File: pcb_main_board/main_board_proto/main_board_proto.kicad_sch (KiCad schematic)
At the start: 35 parts, among them J1 Sortie Moteur 1, J10 L298N 2, J11 L298N 3, J12 IN M2, J13 IN M3, J14 Conn M2, J15 Conn M3, J16 Ardu_M2, J17 Ardu_M3, J18 Entree puissance, J19 output ext 2, J2 L298N 1, J20 button ON/OFF, J3 Conn M1, J4 Ardu_alim, J5 Output ext 1, J6 Ardu_M1, J7 IN M1, J8 Sortie Moteur 2, J9 Sortie Moteur 3, U1 TSR1-2450E, U2 TSR1-2450E, U3 TSR1-2450E

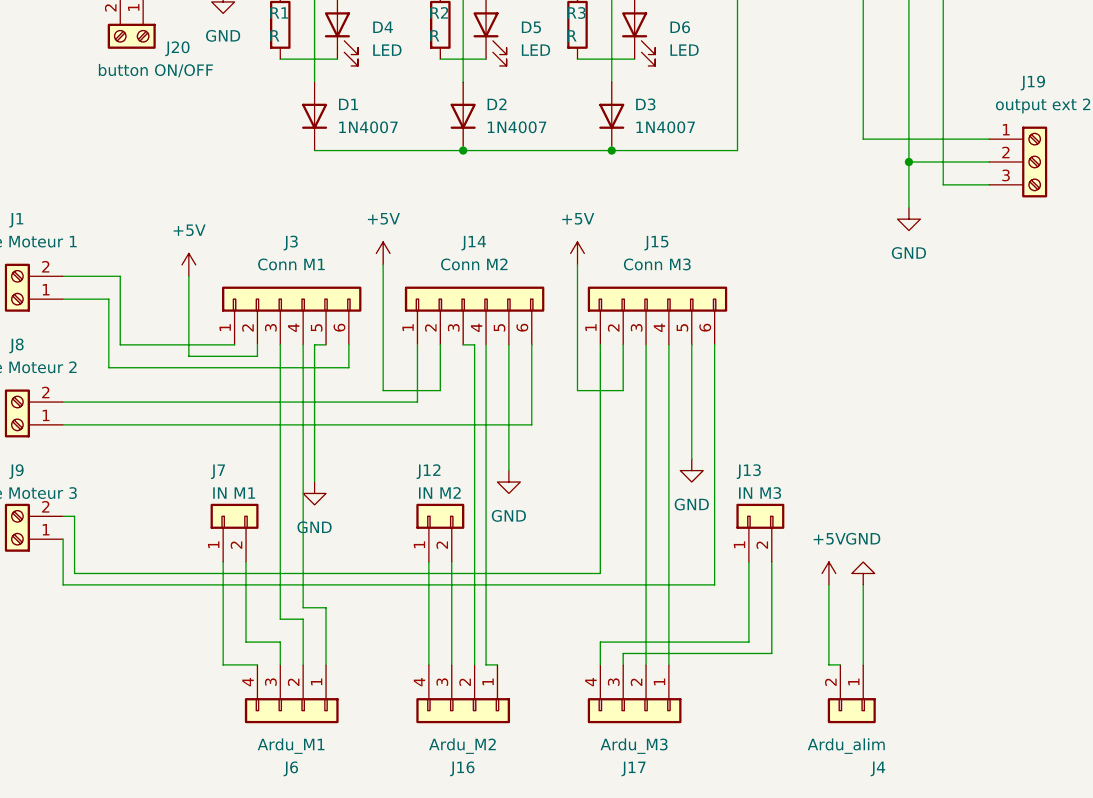
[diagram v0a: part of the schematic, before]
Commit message: Update main PCB board with 3D step file
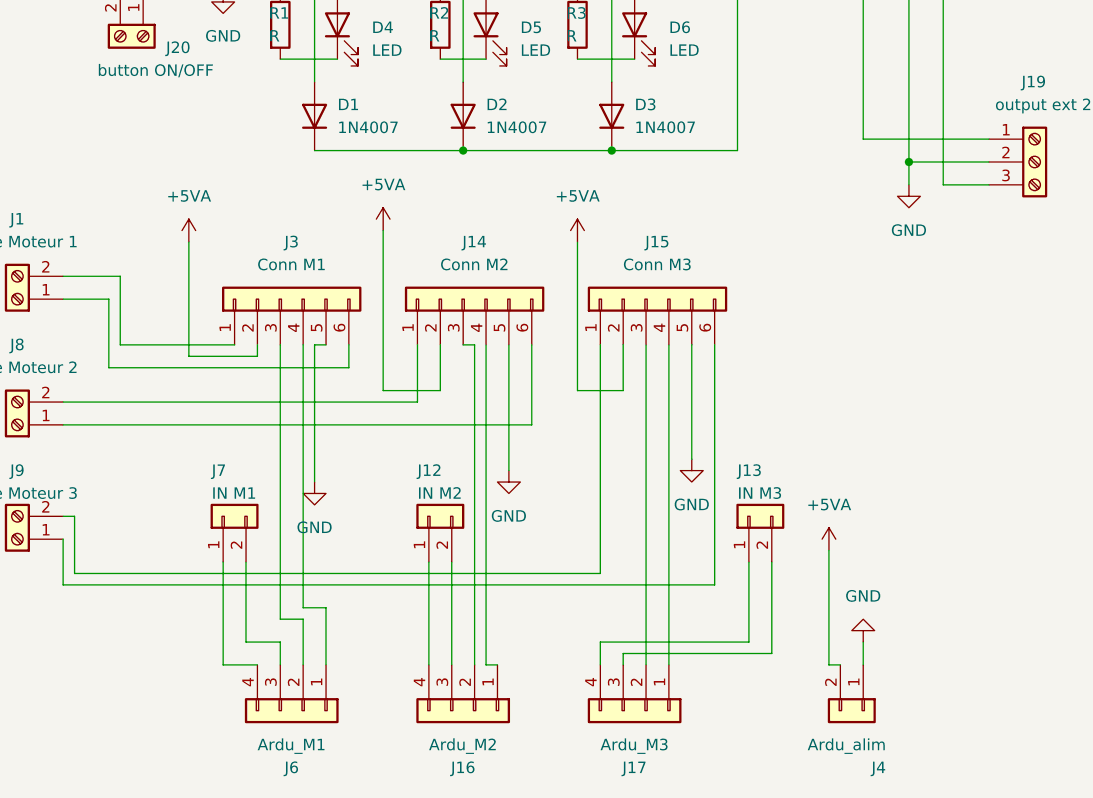
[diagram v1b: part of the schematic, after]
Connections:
- net +5V: no longer J14.2 (Pin_2), J15.2 (Pin_2), J3.2 (Pin_2), J4.2 (Pin_2)
- net +5VA: now also J14.2 (Pin_2), J15.2 (Pin_2), J3.2 (Pin_2), J4.2 (Pin_2)

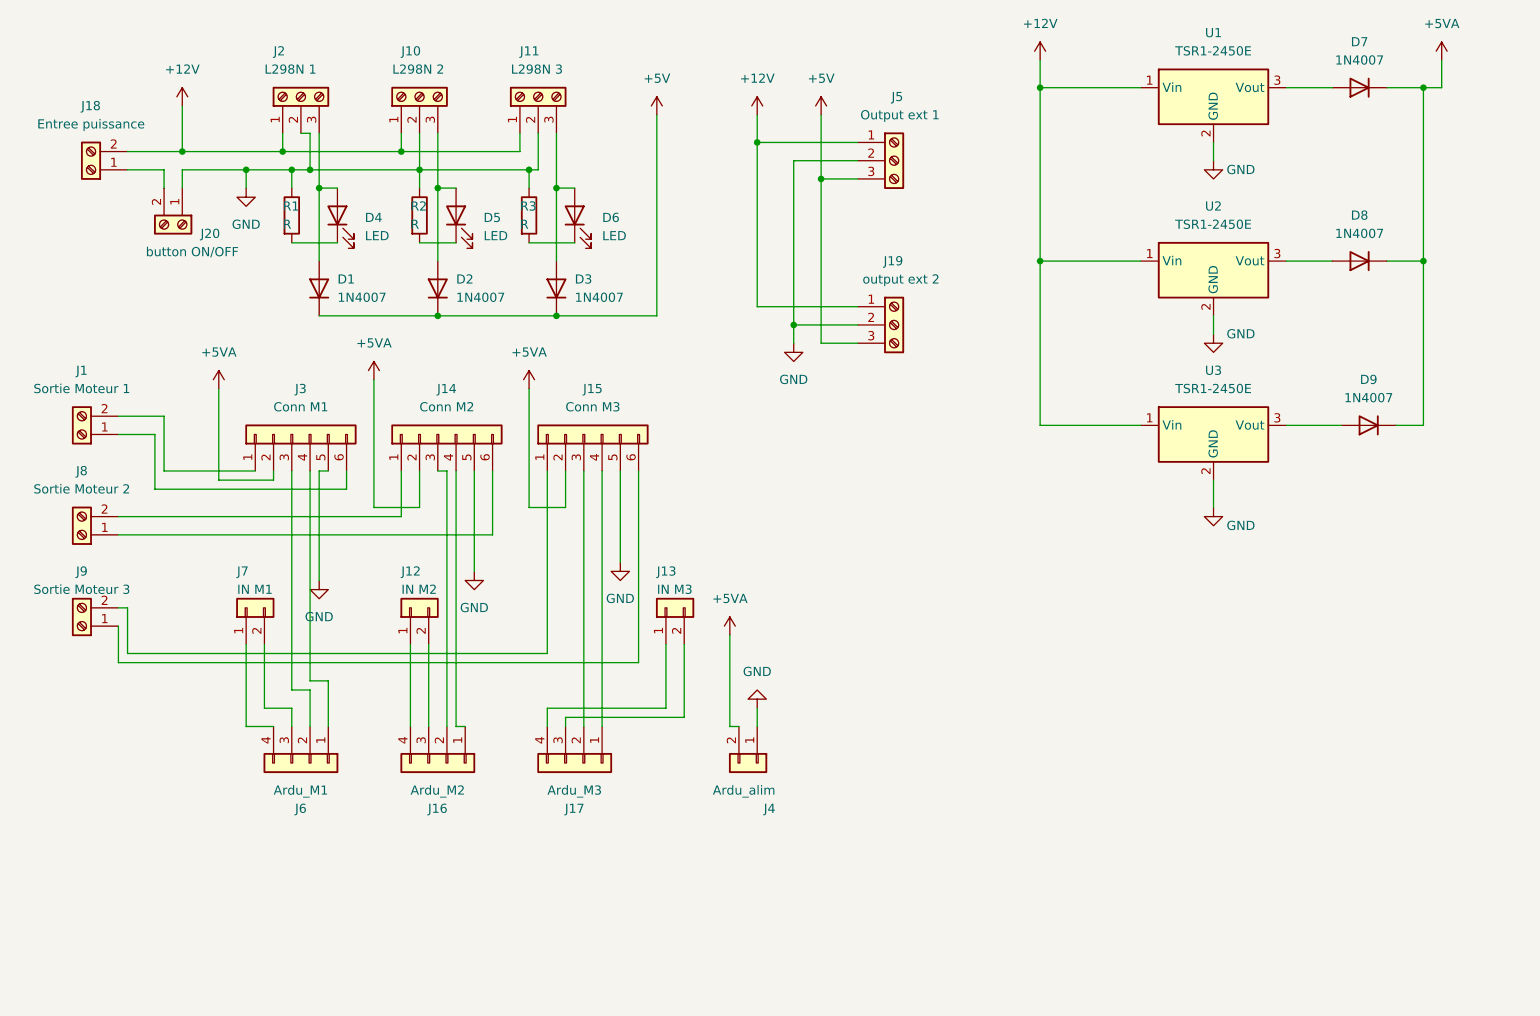
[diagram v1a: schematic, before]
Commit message: Update PCB & Add bom with links to digikey
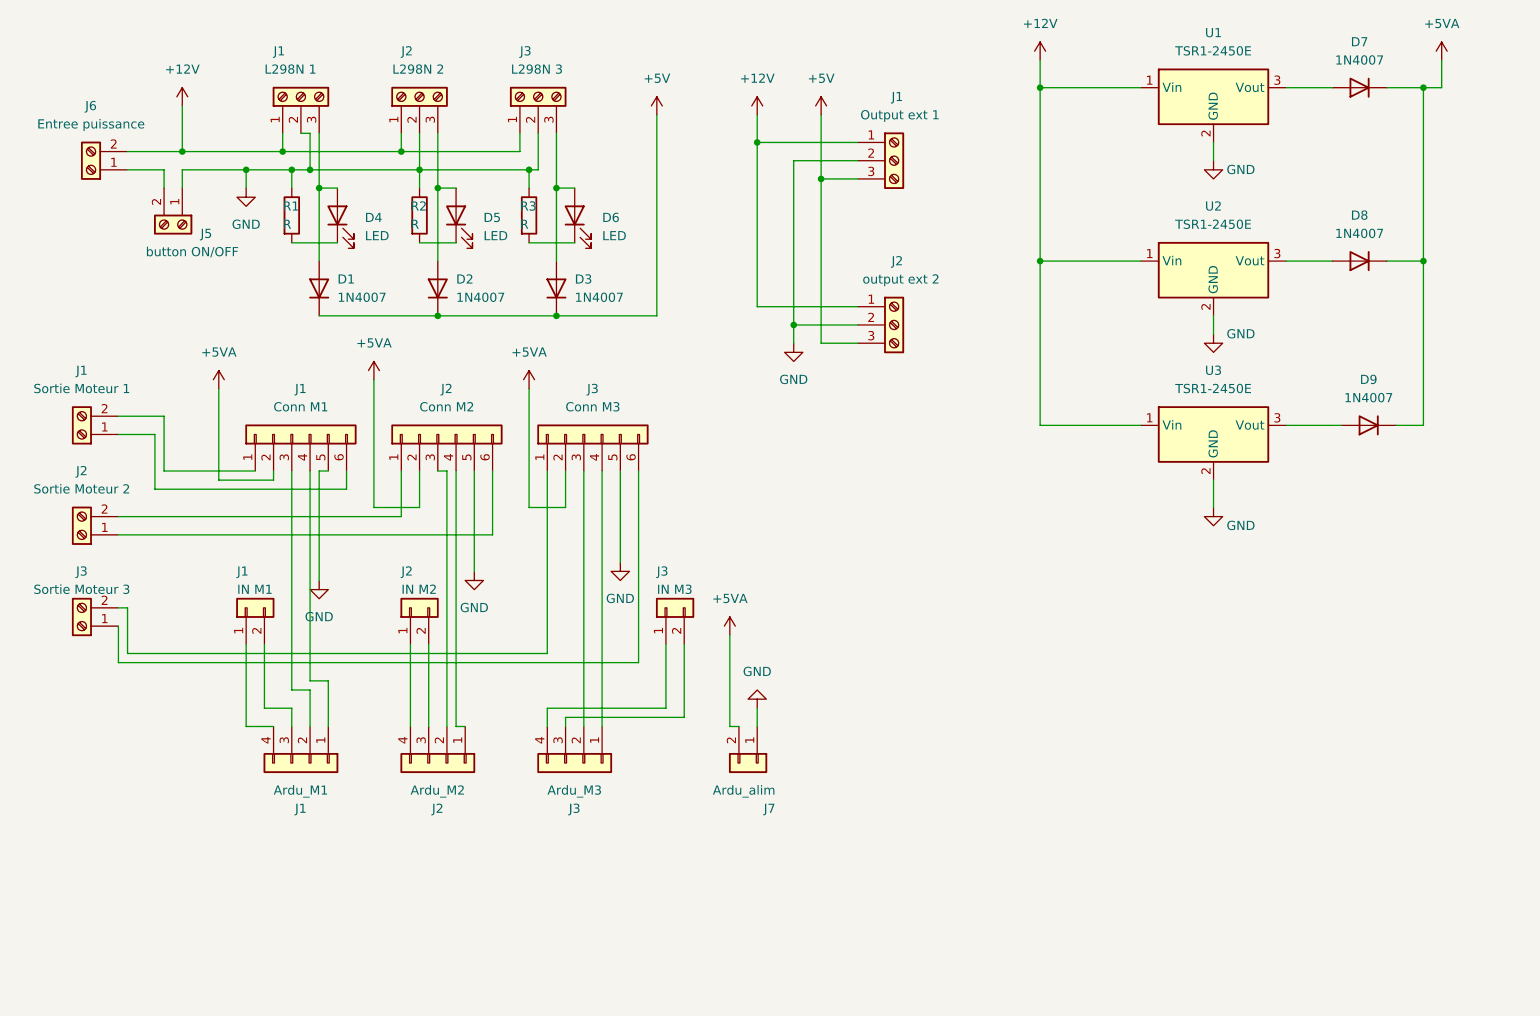
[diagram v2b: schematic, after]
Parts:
- renumbered J5 to J1, J3 to J1, J2 to J1, J6 to J1, J7 to J1, J19 to J2, J10 to J2, J16 to J2, J14 to J2, J8 to J2, J12 to J2, J15 to J3, J17 to J3, J11 to J3, J9 to J3, J13 to J3, J20 to J5, J18 to J6, J4 to J7

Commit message: Adjust main PCB proto v1 with the 3d model step and part in assembly robot
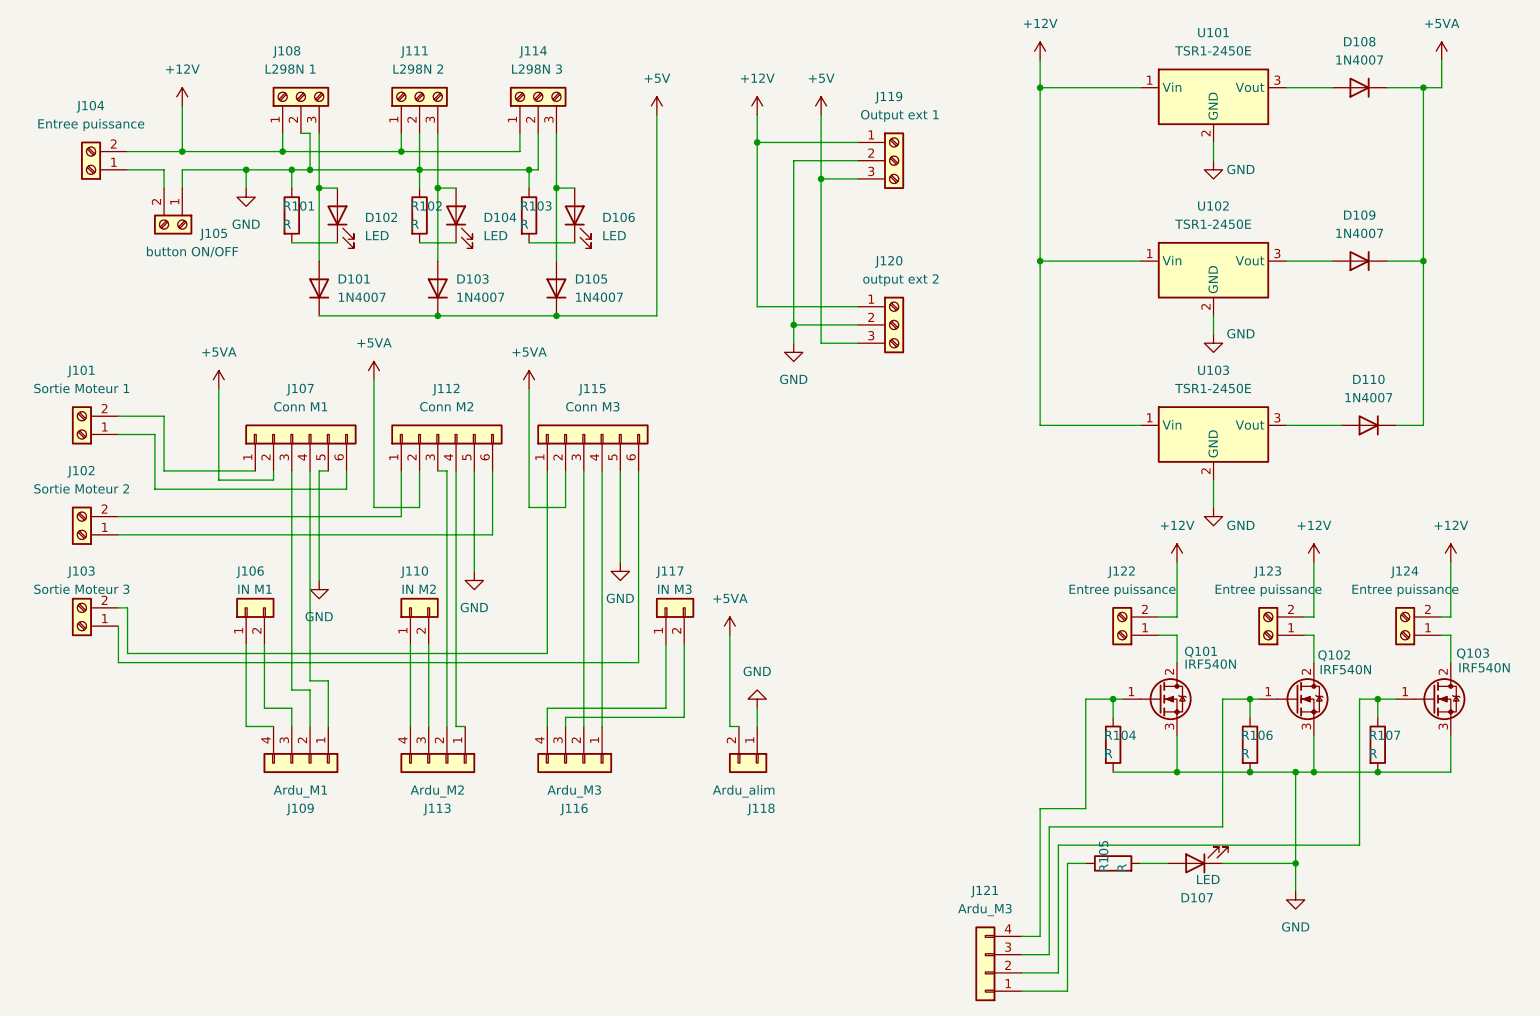
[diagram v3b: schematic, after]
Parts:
- added D107: LED, LED_THT:LED_D5.0mm, symbol Device:LED
- added J121: Ardu_M3, Connector_PinSocket_2.54mm:PinSocket_1x04_P2.54mm_Vertical, symbol Connector_Generic:Conn_01x04
- added J122, J123, J124: Entree puissance, TerminalBlock:TerminalBlock_bornier-2_P5.08mm, symbol Connector:Screw_Terminal_01x02
- added Q101, Q102, Q103: IRF540N, Package_TO_SOT_THT:TO-220-3_Vertical, symbol Transistor_FET:IRF540N
- added R104, R105, R106, R107: R, Resistor_THT:R_Axial_DIN0207_L6.3mm_D2.5mm_P10.16mm_Horizontal, symbol Device:R
- renumbered D1 to D101, D4 to D102, D2 to D103, D5 to D104, D3 to D105, D6 to D106, D7 to D108, D8 to D109, D9 to D110, J1 to J101, J2 to J102, J3 to J103, J6 to J104, J5 to J105, J1 to J106, J1 to J107, J1 to J108, J1 to J109, J2 to J110, J2 to J111, J2 to J112, J2 to J113, J3 to J114, J3 to J115, J3 to J116, J3 to J117, J7 to J118, J1 to J119, J2 to J120, R1 to R101, R2 to R102, R3 to R103, U1 to U101, U2 to U102, U3 to U103
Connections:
- net +12V: now also J122.2 (Pin_2), J123.2 (Pin_2), J124.2 (Pin_2)
- net GND: now also D107.1 (K), Q101.3 (S), Q102.3 (S), Q103.3 (S), R104.2, R106.2, R107.2
- new net: J121.3 (Pin_3), Q102.1 (G), R106.1
- new net: J123.1 (Pin_1), Q102.2 (D)
- new net: D107.2 (A), R105.2
- new net: J121.1 (Pin_1), R105.1
- new net: J121.4 (Pin_4), Q101.1 (G), R104.1
- new net: J122.1 (Pin_1), Q101.2 (D)
- new net: J121.2 (Pin_2), Q103.1 (G), R107.1
- new net: J124.1 (Pin_1), Q103.2 (D)
